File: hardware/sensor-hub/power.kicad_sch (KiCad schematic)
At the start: 11 parts, among them J4 Conn_01x04, U3 AP3402

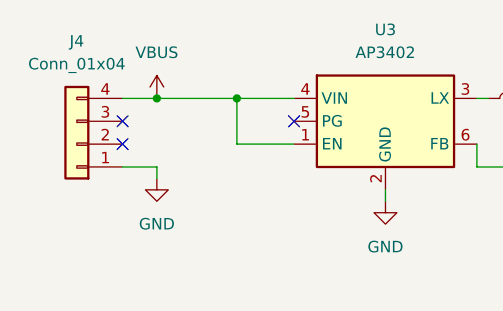
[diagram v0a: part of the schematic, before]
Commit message: Change crystal packages, assign footprints
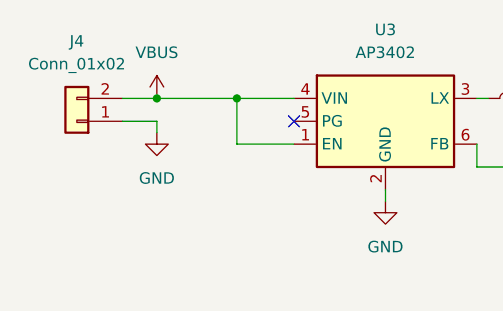
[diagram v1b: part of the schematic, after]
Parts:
- removed J4: Conn_01x04, symbol Connector_Generic:Conn_01x04
- added J4: Conn_01x02, Connector_PinHeader_2.54mm:PinHeader_1x02_P2.54mm_Vertical, symbol Connector_Generic:Conn_01x02
- C23: footprint (none) -> Capacitor_SMD:C_0603_1608Metric
- C24, C25: footprint (none) -> Capacitor_SMD:C_0805_2012Metric
- D3: footprint (none) -> LED_SMD:LED_0603_1608Metric
- R12, R13, R14, R29: footprint (none) -> Resistor_SMD:R_0603_1608Metric
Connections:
- net GND: now also J4.1 (Pin_1)
- net VBUS: now also J4.2 (Pin_2)
- no-connect marks 3 -> 1
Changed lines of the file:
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@@
-	)
-	(no_connect
-		(at 50.8 55.88)
-	)
-	(no_connect
-		(at 50.8 53.34)
 	)
 	(no_connect
@@
 	(wire
 		(pts
-			(xy 50.8 58.42) (xy 54.61 58.42)
+			(xy 50.8 53.34) (xy 54.61 53.34)
 		)
 		(stroke
@@
 	(wire
 		(pts
-			(xy 54.61 58.42) (xy 54.61 59.69)
+			(xy 54.61 53.34) (xy 54.61 54.61)
 		)
 		(stroke
@@
 	(symbol
 		(lib_id "power:GND")
-		(at 54.61 59.69 0)
+		(at 54.61 54.61 0)
 		(unit 1)
 		(exclude_from_sim no)
@@
 		(fields_autoplaced yes)
 		(property "Reference" "#PWR36"
-			(at 54.61 66.04 0)
+			(at 54.61 60.96 0)
 			(effects
 				(font
@@
 		)
 		(property "Value" "GND"
-			(at 54.61 64.77 0)
+			(at 54.61 59.69 0)
 			(effects
 				(font
@@
 		)
 		(property "Footprint" ""
-			(at 54.61 59.69 0)
+			(at 54.61 54.61 0)
 			(effects
 				(font
@@
 		)
 		(property "Datasheet" ""
-			(at 54.61 59.69 0)
+			(at 54.61 54.61 0)
 			(effects
 				(font
@@
 		)
 		(property "Description" "Power symbol creates a global label with name \"GND\" , ground"
-			(at 54.61 59.69 0)
+			(at 54.61 54.61 0)
 			(effects
 				(font
@@
 			)
 		)
-		(property "Footprint" ""
+		(property "Footprint" "Resistor_SMD:R_0603_1608Metric"
 			(at 120.65 62.23 0)
 			(effects
@@
 			)
 		)
-		(property "Footprint" ""
+		(property "Footprint" "Resistor_SMD:R_0603_1608Metric"
 			(at 143.51 50.8 0)
 			(effects
@@
 			)
 		)
-		(property "Footprint" ""
+		(property "Footprint" "Resistor_SMD:R_0603_1608Metric"
 			(at 109.22 62.23 0)
 			(effects
@@
 			)
 		)
-		(property "Footprint" ""
+		(property "Footprint" "Resistor_SMD:R_0603_1608Metric"
 			(at 109.22 54.61 0)
 			(effects
@@
 			)
 		)
-		(property "Footprint" ""
+		(property "Footprint" "Capacitor_SMD:C_0603_1608Metric"
 			(at 100.33 54.61 0)
 			(effects
@@
 			)
 		)
-		(property "Footprint" ""
+		(property "Footprint" "LED_SMD:LED_0603_1608Metric"
 			(at 120.65 54.61 0)
 			(effects
@@
 	)
 	(symbol
+		(lib_id "Connector_Generic:Conn_01x02")
+		(at 45.72 53.34 180)
+		(unit 1)
+		(exclude_from_sim no)
+		(in_bom yes)
+		(on_board yes)
+		(dnp no)
+		(fields_autoplaced yes)
+		(property "Reference" "J4"
+			(at 45.72 44.45 0)
+			(effects
+				(font
+					(size 1.27 1.27)
+				)
+			)
+		)
+		(property "Value" "Conn_01x02"
+			(at 45.72 46.99 0)
+			(effects
+				(font
+					(size 1.27 1.27)
+				)
+			)
+		)
+		(property "Footprint" "Connector_PinHeader_2.54mm:PinHeader_1x02_P2.54mm_Vertical"
+			(at 45.72 53.34 0)
+			(effects
+				(font
+					(size 1.27 1.27)
+				)
+				(hide yes)
+			)
+		)
+		(property "Datasheet" "~"
+			(at 45.72 53.34 0)
+			(effects
+				(font
+					(size 1.27 1.27)
+				)
+				(hide yes)
+			)
+		)
+		(property "Description" "Generic connector, single row, 01x02, script generated (kicad-library-utils/schlib/autogen/connector/)"
+			(at 45.72 53.34 0)
+			(effects
+				(font
+					(size 1.27 1.27)
+				)
+				(hide yes)
+			)
+		)
+		(pin "2"
+		)
+		(pin "1"
+		)
+		(instances
+			(project ""
+				(path "/e168ef7b-16e4-493f-b63c-2f69374fc890/c562e511-fbc7-4452-9534-9d8032eb5f27"
+					(reference "J4")
+					(unit 1)
+				)
+			)
+		)
+	)
+	(symbol
 		(lib_id "power:GND")
 		(at 80.01 62.23 0)
@@
 	)
 	(symbol
-		(lib_id "Connector_Generic:Conn_01x04")
-		(at 45.72 55.88 180)
-		(unit 1)
-		(exclude_from_sim no)
-		(in_bom yes)
-		(on_board yes)
-		(dnp no)
-		(fields_autoplaced yes)
-		(property "Reference" "J4"
-			(at 45.72 44.45 0)
-			(effects
-				(font
-					(size 1.27 1.27)
-				)
-			)
-		)
-		(property "Value" "Conn_01x04"
-			(at 45.72 46.99 0)
-			(effects
-				(font
-					(size 1.27 1.27)
-				)
-			)
-		)
-		(property "Footprint" ""
-			(at 45.72 55.88 0)
-			(effects
-				(font
-					(size 1.27 1.27)
-				)
-				(hide yes)
-			)
-		)
-		(property "Datasheet" "~"
-			(at 45.72 55.88 0)
-			(effects
-				(font
-					(size 1.27 1.27)
-				)
-				(hide yes)
-			)
-		)
-		(property "Description" "Generic connector, single row, 01x04, script generated (kicad-library-utils/schlib/autogen/connector/)"
-			(at 45.72 55.88 0)
-			(effects
-				(font
-					(size 1.27 1.27)
-				)
-				(hide yes)
-			)
-		)
-		(pin "4"
-		)
-		(pin "1"
-		)
-		(pin "2"
-		)
-		(pin "3"
-		)
-		(instances
-			(project ""
-				(path "/e168ef7b-16e4-493f-b63c-2f69374fc890/c562e511-fbc7-4452-9534-9d8032eb5f27"
-					(reference "J4")
-					(unit 1)
-				)
-			)
-		)
-	)
-	(symbol
 		(lib_id "power:+3V3")
 		(at 148.59 50.8 0)
@@
 			)
 		)
-		(property "Footprint" ""
+		(property "Footprint" "Capacitor_SMD:C_0805_2012Metric"
 			(at 130.81 54.61 0)
 			(effects
@@
 			)
 		)
-		(property "Footprint" ""
+		(property "Footprint" "Capacitor_SMD:C_0805_2012Metric"
 			(at 139.7 54.61 0)
 			(effects

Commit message: Assign remaining footprints, change HT sensor
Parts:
- L1: footprint (none) -> Inductor_SMD:L_APV_ANR5045
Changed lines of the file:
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@@
 			)
 		)
-		(property "Footprint" ""
+		(property "Footprint" "Inductor_SMD:L_APV_ANR5045"
 			(at 95.25 50.8 0)
 			(effects

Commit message: Start layout
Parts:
- added C42: 22u, Capacitor_SMD:C_0805_2012Metric, symbol Device:C_Small
- added C43: 100n, Capacitor_SMD:C_0603_1608Metric, symbol Device:C_Small
- J4: value Conn_01x02 -> PWR
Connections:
- net GND: now also C42.2, C43.2
- net VBUS: now also C42.1, C43.1
- net +3V3 renamed +3.3V
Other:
- moved on the sheet: J4

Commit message: Core layout done
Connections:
- net 3.3V_P0: now reaches C23.1, C24.1, C25.1, D3.2 (A), L1.2, R12.1, R14.1
- net LX: now reaches L1.1, U3.3 (LX)
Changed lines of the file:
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@@
+		)
+	)
+	(label "3.3V_P0"
+		(at 111.76 50.8 0)
+		(effects
+			(font
+				(size 1.27 1.27)
+			)
+			(justify left bottom)
+		)
+	)
+	(label "LX"
+		(at 90.17 50.8 0)
+		(effects
+			(font
+				(size 1.27 1.27)
+			)
+			(justify left bottom)
 		)
 	)

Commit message: Finalize layout
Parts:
- added C44: 10u, Capacitor_SMD:C_0805_2012Metric, symbol Device:C_Small
- added C45, C46: 22u, Capacitor_SMD:C_0805_2012Metric, symbol Device:C_Small
- added D4: LED, LED_SMD:LED_0603_1608Metric, symbol Device:LED
- added R38: 1k, Resistor_SMD:R_0603_1608Metric, symbol Device:R_Small
- added U6: AMS1117-3.3, Package_TO_SOT_SMD:SOT-223-3_TabPin2, symbol Regulator_Linear:AMS1117-3.3
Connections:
- net GND: now also C44.2, C45.2, C46.2, R38.2, U6.1 (GND)
- net VBUS: now also C44.1, U6.3 (VI)
- new net: D4.1 (K), R38.1
- new net +3.3V_LDO: C45.1, C46.1, D4.2 (A), U6.2 (VO)
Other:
- note added: "LDO for sensors"
- note added: "Main 3.3V DC/DC"
